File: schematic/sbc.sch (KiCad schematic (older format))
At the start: 12 parts

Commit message: sbc schematic update. This version appears to boot
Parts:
- added R?: 3.3k, symbol Rsqig
- R? (x5): value 3.3 -> 3.3k
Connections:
- wire segments 26 -> 27
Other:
- moved on the sheet: R?
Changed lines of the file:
@@
 L Rsqig R?
 U 1 1 5819F9A1
-P 3500 1000
-F 0 "R?" V 3550 850 50  0000 C CNN
-F 1 "3.3" V 3425 1000 50  0000 C CNN
-F 2 "" V 3430 1000 50  0000 C CNN
-F 3 "" H 3500 1000 50  0000 C CNN
-	1    3500 1000
-	1    0    0    -1
+P 2825 3800
+F 0 "R?" V 2875 3650 50  0000 C CNN
+F 1 "3.3k" V 2750 3800 50  0000 C CNN
+F 2 "" V 2755 3800 50  0000 C CNN
+F 3 "" H 2825 3800 50  0000 C CNN
+	1    2825 3800
+	0    -1   -1   0
 $EndComp
 Text GLabel 875  775  0    60   Input ~ 0
@@
 P 3350 1000
 F 0 "R?" V 3400 850 50  0000 C CNN
-F 1 "3.3" V 3275 1000 50  0000 C CNN
+F 1 "3.3k" V 3275 1000 50  0000 C CNN
 F 2 "" V 3280 1000 50  0000 C CNN
 F 3 "" H 3350 1000 50  0000 C CNN
@@
 P 3200 1000
 F 0 "R?" V 3250 850 50  0000 C CNN
-F 1 "3.3" V 3125 1000 50  0000 C CNN
+F 1 "3.3k" V 3125 1000 50  0000 C CNN
 F 2 "" V 3130 1000 50  0000 C CNN
 F 3 "" H 3200 1000 50  0000 C CNN
@@
 Wire Wire Line
 	3350 3700 3350 1150
-Wire Wire Line
-	2550 3800 3500 3800
-Wire Wire Line
-	3500 3800 3500 1150
 $Comp
 L Rsqig R?
@@
 P 3050 1000
 F 0 "R?" V 3100 850 50  0000 C CNN
-F 1 "3.3" V 2975 1000 50  0000 C CNN
+F 1 "3.3k" V 2975 1000 50  0000 C CNN
 F 2 "" V 2980 1000 50  0000 C CNN
 F 3 "" H 3050 1000 50  0000 C CNN
@@
 P 2900 1000
 F 0 "R?" V 2950 850 50  0000 C CNN
-F 1 "3.3" V 2825 1000 50  0000 C CNN
+F 1 "3.3k" V 2825 1000 50  0000 C CNN
 F 2 "" V 2830 1000 50  0000 C CNN
 F 3 "" H 2900 1000 50  0000 C CNN
@@
 	1050 3600 1050 1675
 NoConn ~ 2550 3150
-NoConn ~ 2550 3900
 NoConn ~ 2550 4000
 NoConn ~ 2550 4100
@@
 F1 "power.sch" 60
 $EndSheet
+Wire Wire Line
+	2550 3800 2675 3800
+NoConn ~ 3000 3800
+$Comp
+L Rsqig R?
+U 1 1 581B7C70
+P 3500 1000
+F 0 "R?" V 3550 850 50  0000 C CNN
+F 1 "3.3k" V 3425 1000 50  0000 C CNN
+F 2 "" V 3430 1000 50  0000 C CNN
+F 3 "" H 3500 1000 50  0000 C CNN
+	1    3500 1000
+	1    0    0    -1
+$EndComp
+Wire Wire Line
+	2550 3900 3500 3900
+Wire Wire Line
+	3500 3900 3500 1150
 $EndSCHEMATC

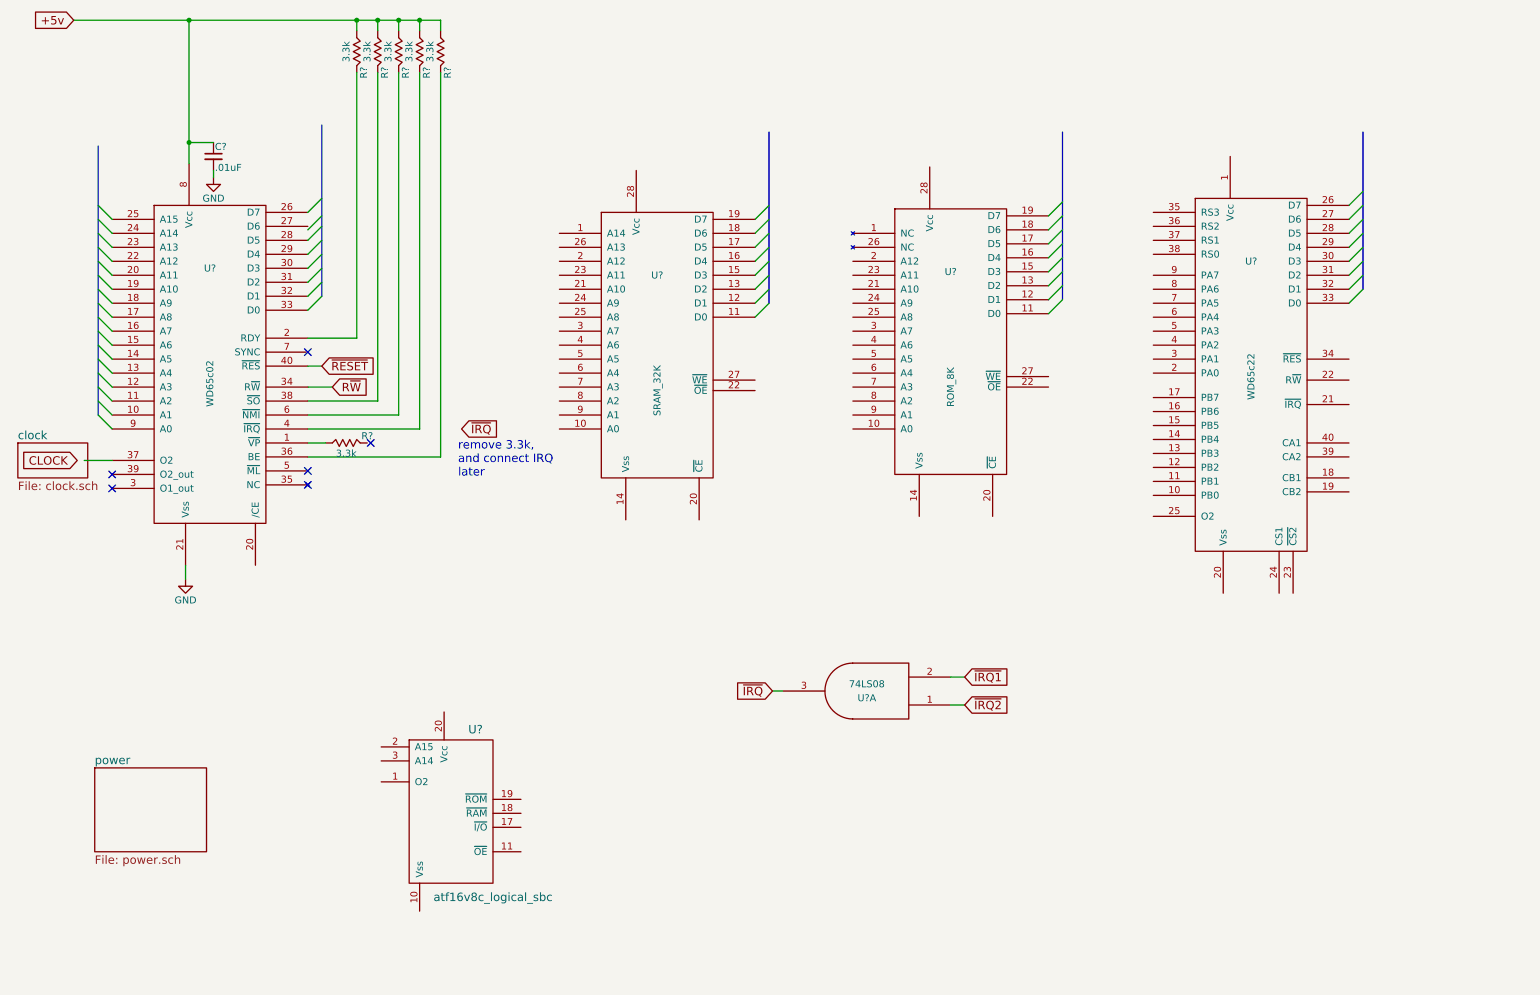
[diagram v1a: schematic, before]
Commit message: sbc schematic update. SPLD connected
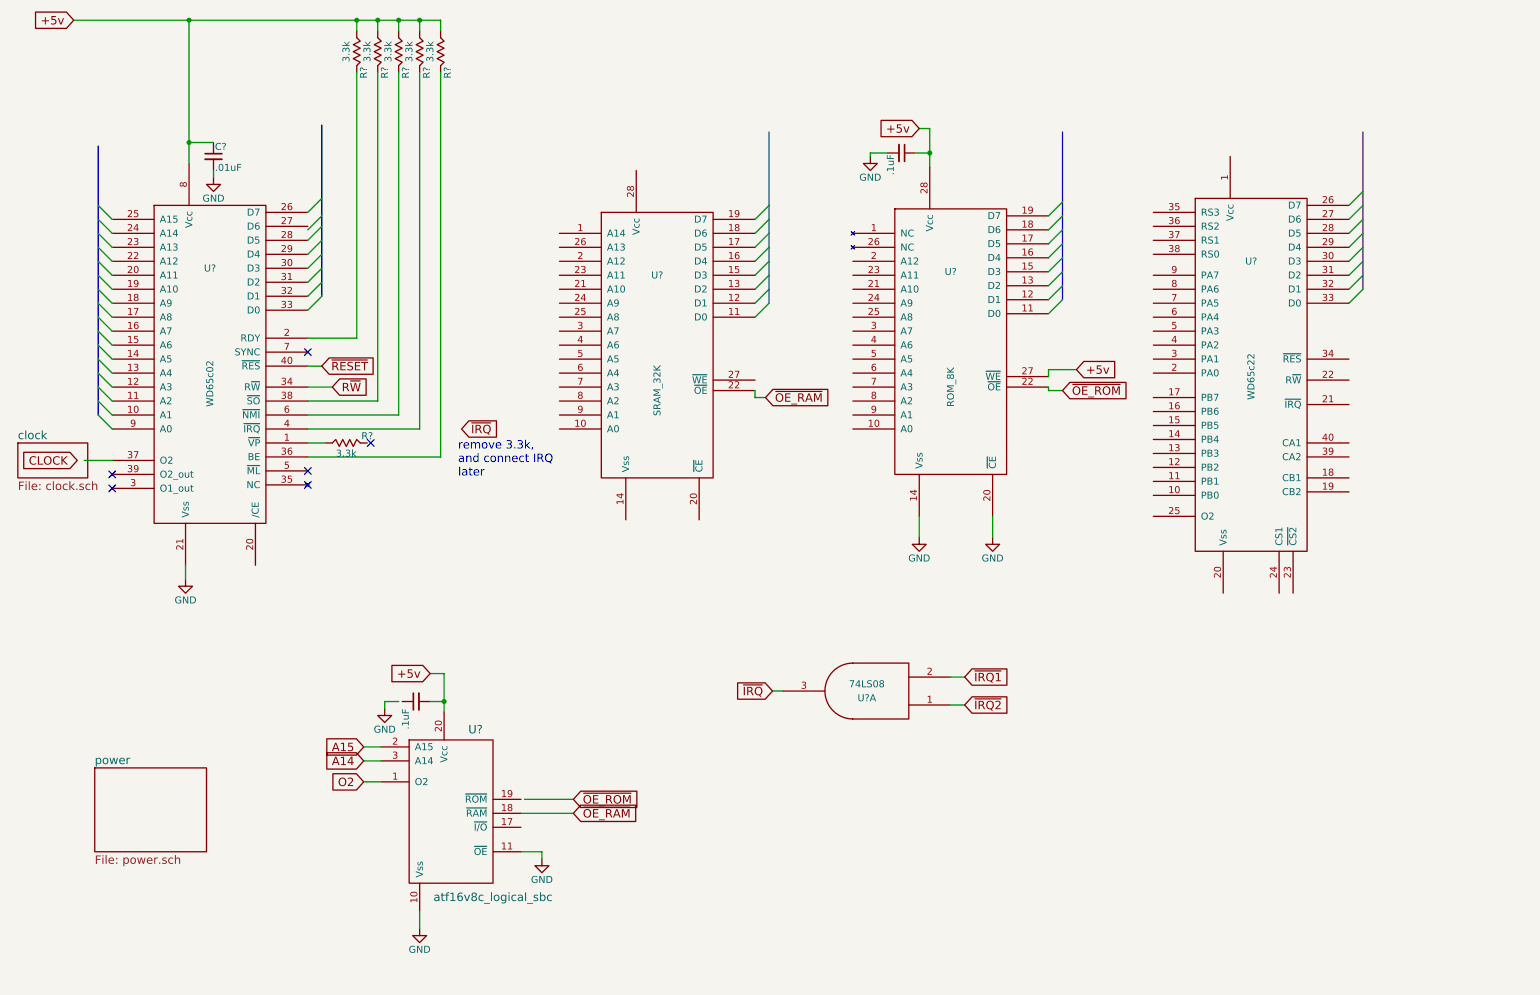
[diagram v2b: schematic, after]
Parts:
- added C? (x2): .1uF, symbol C_Small
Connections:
- net labels added: A14, A15, O2, ~OE_RAM~, ~OE_ROM~
- wire segments 27 -> 53
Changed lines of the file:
@@
 Entry Wire Line
 	10000 2100 10100 2000
-Wire Bus Line
-	10100 1575 10100 2700
-Wire Bus Line
-	7950 1575 7950 2775
-Wire Bus Line
-	5850 1575 5850 2800
-Wire Bus Line
-	2650 1525 2650 2750
 Text GLabel 3650 3700 2    60   Input ~ 0
 ~IRQ~
@@
 Text GLabel 5875 5575 0    60   Input ~ 0
 ~IRQ~
-Wire Wire Line
-	5875 5575 5950 5575
 Text GLabel 7250 5475 2    60   Input ~ 0
 ~IRQ1~
 Text GLabel 7250 5675 2    60   Input ~ 0
 ~IRQ2~
-Wire Wire Line
-	7150 5475 7250 5475
-Wire Wire Line
-	7150 5675 7250 5675
 $Comp
 L Rsqig R?
@@
 	1    0    0    -1
 $EndComp
-Wire Wire Line
-	3350 3700 3350 1150
 $Comp
 L Rsqig R?
@@
 	1    0    0    -1
 $EndComp
-Wire Wire Line
-	2550 3600 3200 3600
-Wire Wire Line
-	3200 3600 3200 1150
-Wire Wire Line
-	2550 3700 3350 3700
 $Comp
 L Rsqig R?
@@
 	1    0    0    -1
 $EndComp
-Wire Wire Line
-	2550 3050 2900 3050
-Wire Wire Line
-	2550 3500 3050 3500
-Wire Wire Line
-	3050 3500 3050 1150
 Text GLabel 2650 3250 2    60   Input ~ 0
 ~RESET~
 Text GLabel 2725 3400 2    60   Input ~ 0
 R~W~
-Wire Wire Line
-	2550 3400 2725 3400
-Wire Wire Line
-	2550 3250 2650 3250
-Wire Wire Line
-	1700 1800 1700 775
-Wire Wire Line
-	875  775  3500 775
-Connection ~ 1700 775
-Wire Wire Line
-	2900 3050 2900 1150
-Wire Wire Line
-	3500 775  3500 850
-Wire Wire Line
-	3350 850  3350 775
-Connection ~ 3350 775
-Connection ~ 3200 775
-Wire Wire Line
-	3050 850  3050 775
-Connection ~ 3050 775
-Wire Wire Line
-	2900 850  2900 775
-Connection ~ 2900 775
-Wire Wire Line
-	3200 850  3200 775
 Entry Wire Line
 	1050 2100 1150 2200
@@
 Entry Wire Line
 	1050 3600 1150 3700
-Wire Bus Line
-	1050 3600 1050 1675
 NoConn ~ 2550 3150
 NoConn ~ 2550 4000
@@
 Text GLabel 900  3925 0    60   Input ~ 0
 CLOCK
-Wire Wire Line
-	950  3925 1150 3925
 $Sheet
 S 475  3800 500  250
@@
 	1    0    0    -1
 $EndComp
-Wire Wire Line
-	1675 4775 1675 4675
 $Comp
 L C_Small C?
@@
 	1    0    0    -1
 $EndComp
-Wire Wire Line
-	1875 1650 1700 1650
-Connection ~ 1700 1650
-Wire Wire Line
-	1875 1900 1875 1850
 $Sheet
 S 1025 6125 800  600
@@
 F1 "power.sch" 60
 $EndSheet
-Wire Wire Line
-	2550 3800 2675 3800
 NoConn ~ 3000 3800
 $Comp
@@
 	1    0    0    -1
 $EndComp
+Text GLabel 4450 6350 2    60   Input ~ 0
+~OE_ROM~
+Text GLabel 4450 6450 2    60   Input ~ 0
+~OE_RAM~
+Text GLabel 7950 3425 2    60   Input ~ 0
+~OE_ROM~
+Text GLabel 5825 3475 2    60   Input ~ 0
+~OE_RAM~
+Wire Bus Line
+	10100 1575 10100 2700
+Wire Bus Line
+	7950 1575 7950 2775
+Wire Bus Line
+	5850 1575 5850 2800
+Wire Bus Line
+	2650 1525 2650 2750
+Wire Wire Line
+	5875 5575 5950 5575
+Wire Wire Line
+	7150 5475 7250 5475
+Wire Wire Line
+	7150 5675 7250 5675
+Wire Wire Line
+	3350 3700 3350 1150
+Wire Wire Line
+	2550 3600 3200 3600
+Wire Wire Line
+	3200 3600 3200 1150
+Wire Wire Line
+	2550 3050 2900 3050
+Wire Wire Line
+	2550 3500 3050 3500
+Wire Wire Line
+	3050 3500 3050 1150
+Wire Wire Line
+	2550 3400 2725 3400
+Wire Wire Line
+	2550 3250 2650 3250
+Wire Wire Line
+	1700 1800 1700 775
+Wire Wire Line
+	875  775  3500 775
+Connection ~ 1700 775
+Wire Wire Line
+	2900 3050 2900 1150
+Wire Wire Line
+	3500 775  3500 850
+Wire Wire Line
+	3350 850  3350 775
+Connection ~ 3350 775
+Connection ~ 3200 775
+Wire Wire Line
+	3050 850  3050 775
+Connection ~ 3050 775
+Wire Wire Line
+	2900 850  2900 775
+Connection ~ 2900 775
+Wire Wire Line
+	3200 850  3200 775
+Wire Bus Line
+	1050 3600 1050 1675
+Wire Wire Line
+	950  3925 1150 3925
+Wire Wire Line
+	1675 4775 1675 4675
+Wire Wire Line
+	1875 1650 1700 1650
+Connection ~ 1700 1650
+Wire Wire Line
+	1875 1900 1875 1850
+Wire Wire Line
+	2550 3800 2675 3800
 Wire Wire Line
 	2550 3900 3500 3900
 Wire Wire Line
 	3500 3900 3500 1150
+Wire Wire Line
+	2550 3700 3350 3700
+Wire Wire Line
+	4100 6350 4450 6350
+Wire Wire Line
+	4075 6450 4450 6450
+Wire Wire Line
+	7950 3425 7850 3425
+Wire Wire Line
+	7850 3425 7850 3400
+Wire Wire Line
+	5750 3425 5750 3475
+Wire Wire Line
+	5750 3475 5825 3475
+$Comp
+L GND #PWR?
+U 1 1 582D4637
+P 4225 6775
+F 0 "#PWR?" H 4225 6525 50  0001 C CNN
+F 1 "GND" H 4225 6625 50  0000 C CNN
+F 2 "" H 4225 6775 50  0000 C CNN
+F 3 "" H 4225 6775 50  0000 C CNN
+	1    4225 6775
+	1    0    0    -1
+$EndComp
+$Comp
+L GND #PWR?
+U 1 1 582D4665
+P 3350 7275
+F 0 "#PWR?" H 3350 7025 50  0001 C CNN
+F 1 "GND" H 3350 7125 50  0000 C CNN
+F 2 "" H 3350 7275 50  0000 C CNN
+F 3 "" H 3350 7275 50  0000 C CNN
+	1    3350 7275
+	1    0    0    -1
+$EndComp
+Wire Wire Line
+	3350 7275 3350 7150
+Wire Wire Line
+	4075 6725 4225 6725
+Wire Wire Line
+	4225 6725 4225 6775
+Text GLabel 3425 5450 0    60   Input ~ 0
++5v
+$Comp
+L C_Small C?
+U 1 1 582D474D
+P 3325 5650
+F 0 "C?" H 3335 5720 50  0001 L CNN
+F 1 ".1uF" H 3125 5725 50  0000 L CNN
+F 2 "" H 3325 5650 50  0000 C CNN
+F 3 "" H 3325 5650 50  0000 C CNN
+	1    3325 5650
+	0    -1   -1   0
+$EndComp
+Wire Wire Line
+	3425 5450 3525 5450
+Wire Wire Line
+	3525 5450 3525 5725
+Wire Wire Line
+	3425 5650 3525 5650
+Connection ~ 3525 5650
+$Comp
+L GND #PWR?
+U 1 1 582D4989
+P 3100 5700
+F 0 "#PWR?" H 3100 5450 50  0001 C CNN
+F 1 "GND" H 3100 5550 50  0000 C CNN
+F 2 "" H 3100 5700 50  0000 C CNN
+F 3 "" H 3100 5700 50  0000 C CNN
+	1    3100 5700
+	1    0    0    -1
+$EndComp
+Wire Wire Line
+	3200 5650 3100 5650
+Wire Wire Line
+	3100 5650 3100 5700
+Text GLabel 2950 5975 0    60   Input ~ 0
+A15
+Text GLabel 2950 6075 0    60   Input ~ 0
+A14
+Wire Wire Line
+	2950 5975 3075 5975
+Wire Wire Line
+	2950 6075 3075 6075
+Text GLabel 2950 6225 0    60   Input ~ 0
+O2
+Wire Wire Line
+	2950 6225 3075 6225
+Text GLabel 6925 1550 0    60   Input ~ 0
++5v
+$Comp
+L C_Small C?
+U 1 1 582D4B9C
+P 6800 1725
+F 0 "C?" H 6810 1795 50  0001 L CNN
+F 1 ".1uF" H 6810 1645 50  0000 L CNN
+F 2 "" H 6800 1725 50  0000 C CNN
+F 3 "" H 6800 1725 50  0000 C CNN
+	1    6800 1725
+	0    1    1    0
+$EndComp
+$Comp
+L GND #PWR?
+U 1 1 582D4C2B
+P 6575 1750
+F 0 "#PWR?" H 6575 1500 50  0001 C CNN
+F 1 "GND" H 6575 1600 50  0000 C CNN
+F 2 "" H 6575 1750 50  0000 C CNN
+F 3 "" H 6575 1750 50  0000 C CNN
+	1    6575 1750
+	1    0    0    -1
+$EndComp
+Wire Wire Line
+	6925 1550 7000 1550
+Wire Wire Line
+	7000 1550 7000 1825
+Wire Wire Line
+	6900 1725 7000 1725
+Connection ~ 7000 1725
+Wire Wire Line
+	6700 1725 6575 1725
+Wire Wire Line
+	6575 1725 6575 1750
+$Comp
+L GND #PWR?
+U 1 1 582D4DD8
+P 6925 4475
+F 0 "#PWR?" H 6925 4225 50  0001 C CNN
+F 1 "GND" H 6925 4325 50  0000 C CNN
+F 2 "" H 6925 4475 50  0000 C CNN
+F 3 "" H 6925 4475 50  0000 C CNN
+	1    6925 4475
+	1    0    0    -1
+$EndComp
+$Comp
+L GND #PWR?
+U 1 1 582D4E06
+P 7450 4475
+F 0 "#PWR?" H 7450 4225 50  0001 C CNN
+F 1 "GND" H 7450 4325 50  0000 C CNN
+F 2 "" H 7450 4475 50  0000 C CNN
+F 3 "" H 7450 4475 50  0000 C CNN
+	1    7450 4475
+	1    0    0    -1
+$EndComp
+Wire Wire Line
+	7450 4475 7450 4325
+Wire Wire Line
+	6925 4475 6925 4325
+Text GLabel 8050 3275 2    60   Input ~ 0
++5v
+Wire Wire Line
+	7850 3325 7850 3275
+Wire Wire Line
+	7850 3275 8050 3275
 $EndSCHEMATC
